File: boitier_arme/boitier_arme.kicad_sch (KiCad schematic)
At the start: 7 parts, among them J1 Conn_01x02_Pin, U1 XIAO-nRF52840-SMD

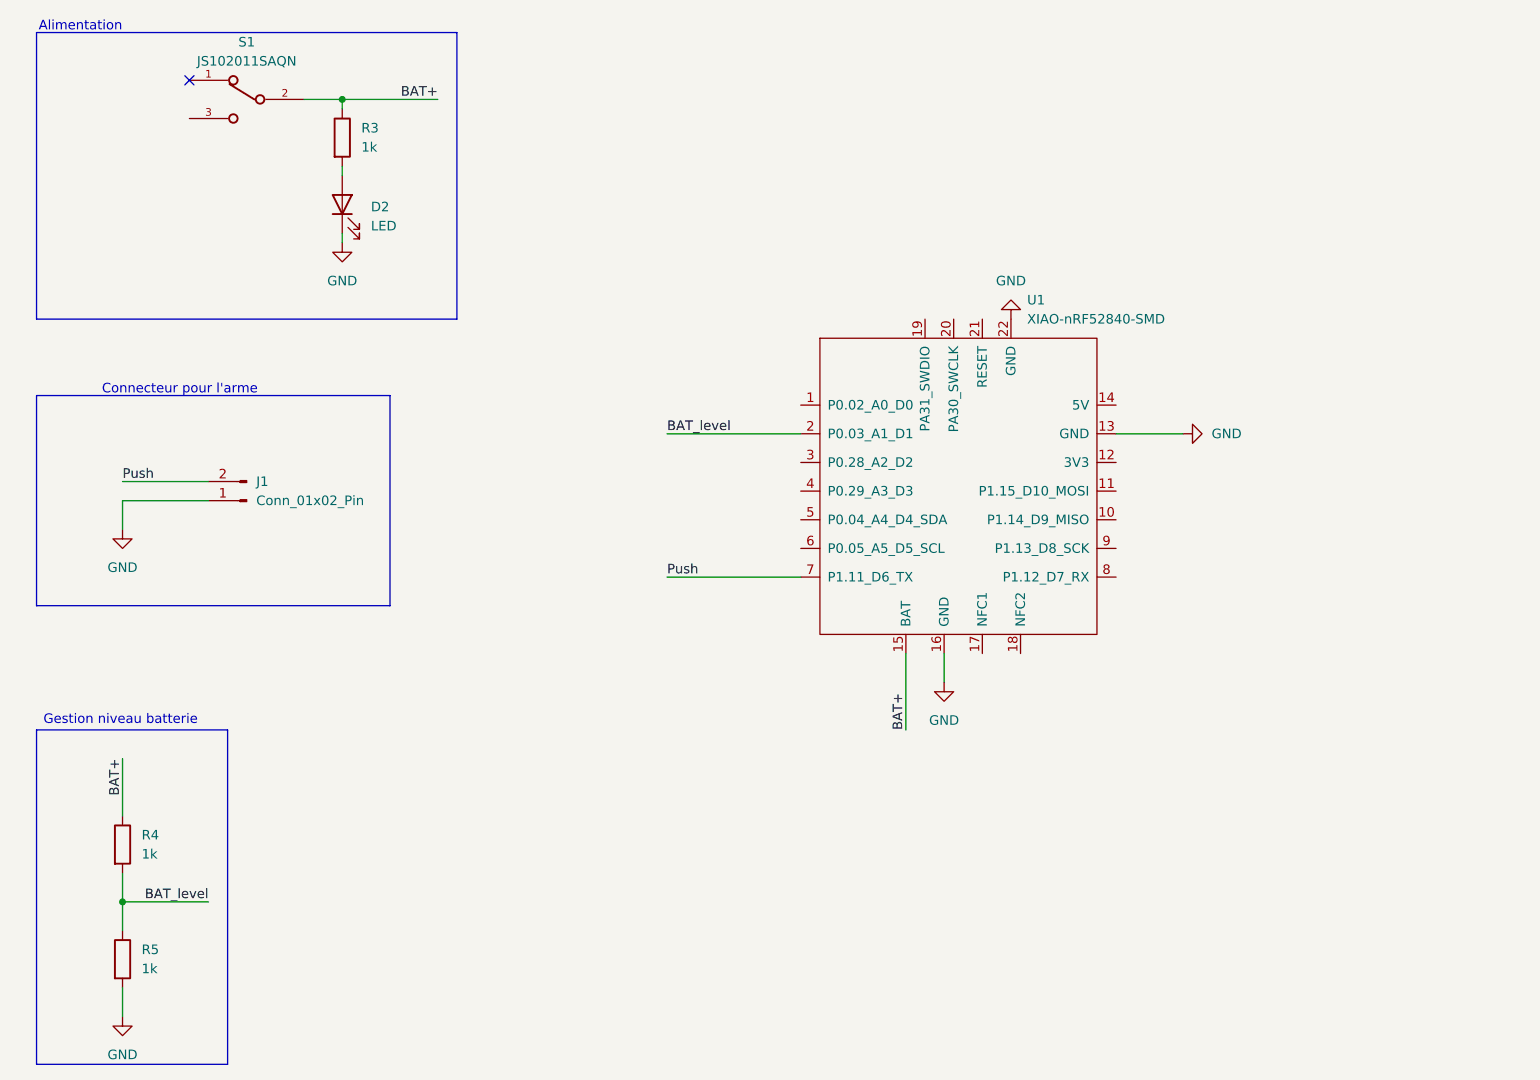
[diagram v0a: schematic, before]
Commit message: batterie rajouté
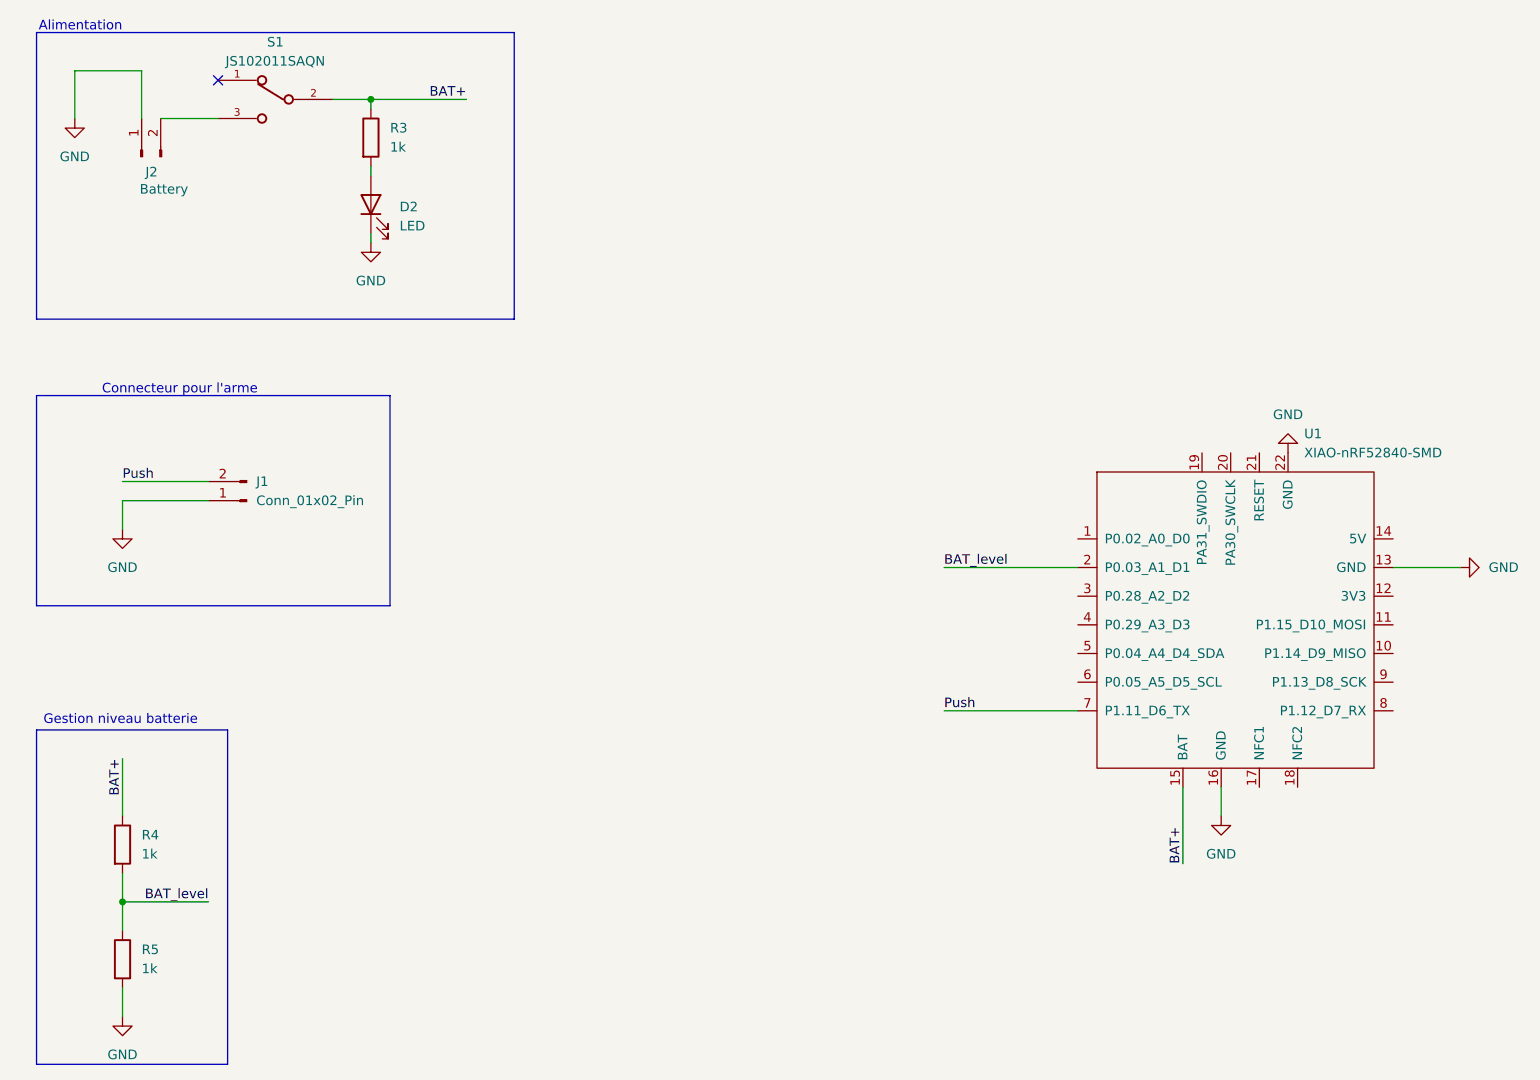
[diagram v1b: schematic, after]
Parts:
- added J2: Battery, Connector_JST:JST_XH_B2B-XH-A_1x02_P2.50mm_Vertical, symbol Connector:Conn_01x02_Pin
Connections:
- net GND: now also J2.1 (Pin_1)
- net at S1.3: now also J2.2 (Pin_2)
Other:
- moved on the sheet: D2, R3, S1, U1

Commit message: a jour
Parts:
- removed J2: Battery, Connector_JST:JST_XH_B2B-XH-A_1x02_P2.50mm_Vertical, symbol Connector:Conn_01x02_Pin
- added J2: 125SH-B-02-TS, CONN_125SH-B-02-TS_ADM, symbol 2025-07-15_01-55-54:125SH-B-02-TS
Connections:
- net GND: now also J2.2
- net at S1.3: now also J2.1
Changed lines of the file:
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@@
+	)
+	(symbol
+		(lib_id "2025-07-15_01-55-54:125SH-B-02-TS")
+		(at 30.48 27.94 270)
+		(unit 1)
+		(exclude_from_sim no)
+		(in_bom yes)
+		(on_board yes)
+		(dnp no)
+		(fields_autoplaced yes)
+		(property "Reference" "J2"
+			(at 34.29 35.5599 90)
+			(effects
+				(font
+					(size 1.524 1.524)
+				)
+				(justify left)
+			)
+		)
+		(property "Value" "125SH-B-02-TS"
+			(at 34.29 38.0999 90)
+			(effects
+				(font
+					(size 1.524 1.524)
+				)
+				(justify left)
+			)
+		)
+		(property "Footprint" "CONN_125SH-B-02-TS_ADM"
+			(at 30.48 27.94 0)
+			(effects
+				(font
+					(size 1.27 1.27)
+					(italic yes)
+				)
+				(hide yes)
+			)
+		)
+		(property "Datasheet" "125SH-B-02-TS"
+			(at 30.48 27.94 0)
+			(effects
+				(font
+					(size 1.27 1.27)
+					(italic yes)
+				)
+				(hide yes)
+			)
+		)
+		(property "Description" ""
+			(at 30.48 27.94 0)
+			(effects
+				(font
+					(size 1.27 1.27)
+				)
+				(hide yes)
+			)
+		)
+		(pin "1"
+		)
+		(pin "2"
+		)
+		(instances
+			(project ""
+				(path "/98d1fd79-24f6-41e8-83f3-a60accf8c857"
+					(reference "J2")
+					(unit 1)
+				)
+			)
+		)
 	)
 	(symbol
@@
 					(unit 1)
 				)
-			)
-		)
-	)
-	(symbol
-		(lib_id "Connector:Conn_01x02_Pin")
-		(at 27.94 33.02 90)
-		(unit 1)
-		(exclude_from_sim no)
-		(in_bom yes)
-		(on_board yes)
-		(dnp no)
-		(property "Reference" "J2"
-			(at 28.448 35.052 90)
-			(effects
-				(font
-					(size 1.27 1.27)
-				)
-				(justify right)
-			)
-		)
-		(property "Value" "Battery"
-			(at 27.686 37.338 90)
-			(effects
-				(font
-					(size 1.27 1.27)
-				)
-				(justify right)
-			)
-		)
-		(property "Footprint" "Connector_JST:JST_XH_B2B-XH-A_1x02_P2.50mm_Vertical"
-			(at 27.94 33.02 0)
-			(effects
-				(font
-					(size 1.27 1.27)
-				)
-				(hide yes)
-			)
-		)
-		(property "Datasheet" "~"
-			(at 27.94 33.02 0)
-			(effects
-				(font
-					(size 1.27 1.27)
-				)
-				(hide yes)
-			)
-		)
-		(property "Description" "Generic connector, single row, 01x02, script generated"
-			(at 27.94 33.02 0)
-			(effects
-				(font
-					(size 1.27 1.27)
-				)
-				(hide yes)
-			)
-		)
-		(pin "1"
-		)
-		(pin "2"
-		)
-		(instances
-			(project "boitier_arme"
-				(path "/98d1fd79-24f6-41e8-83f3-a60accf8c857"
-					(reference "J2")
-					(unit 1)
-				)

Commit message: a jour
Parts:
- J1: footprint Connector_JST:JST_XH_B2B-XH-A_1x02_P2.50mm_Vertical -> Connector_JST:JST_XH_S2B-XH-A-1_1x02_P2.50mm_Horizontal
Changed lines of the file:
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@@
 			)
 		)
-		(property "Footprint" "Connector_JST:JST_XH_B2B-XH-A_1x02_P2.50mm_Vertical"
+		(property "Footprint" "Connector_JST:JST_XH_S2B-XH-A-1_1x02_P2.50mm_Horizontal"
 			(at 41.91 78.74 0)
 			(effects

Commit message: Changement suite au retour du GUS
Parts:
- added H1, H2, H3: MountingHole, MountingHole:MountingHole_3.5mm, symbol Mechanical:MountingHole
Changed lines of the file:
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@@
+	)
+	(symbol
+		(lib_id "Mechanical:MountingHole")
+		(at 92.71 26.67 0)
+		(unit 1)
+		(exclude_from_sim no)
+		(in_bom no)
+		(on_board yes)
+		(dnp no)
+		(fields_autoplaced yes)
+		(property "Reference" "H2"
+			(at 95.25 25.3999 0)
+			(effects
+				(font
+					(size 1.27 1.27)
+				)
+				(justify left)
+			)
+		)
+		(property "Value" "MountingHole"
+			(at 95.25 27.9399 0)
+			(effects
+				(font
+					(size 1.27 1.27)
+				)
+				(justify left)
+			)
+		)
+		(property "Footprint" "MountingHole:MountingHole_3.5mm"
+			(at 92.71 26.67 0)
+			(effects
+				(font
+					(size 1.27 1.27)
+				)
+				(hide yes)
+			)
+		)
+		(property "Datasheet" "~"
+			(at 92.71 26.67 0)
+			(effects
+				(font
+					(size 1.27 1.27)
+				)
+				(hide yes)
+			)
+		)
+		(property "Description" "Mounting Hole without connection"
+			(at 92.71 26.67 0)
+			(effects
+				(font
+					(size 1.27 1.27)
+				)
+				(hide yes)
+			)
+		)
+		(instances
+			(project "boitier_arme"
+				(path "/98d1fd79-24f6-41e8-83f3-a60accf8c857"
+					(reference "H2")
+					(unit 1)
+				)
+			)
+		)
+	)
+	(symbol
+		(lib_id "Mechanical:MountingHole")
+		(at 92.71 21.59 0)
+		(unit 1)
+		(exclude_from_sim no)
+		(in_bom no)
+		(on_board yes)
+		(dnp no)
+		(fields_autoplaced yes)
+		(property "Reference" "H1"
+			(at 95.25 20.3199 0)
+			(effects
+				(font
+					(size 1.27 1.27)
+				)
+				(justify left)
+			)
+		)
+		(property "Value" "MountingHole"
+			(at 95.25 22.8599 0)
+			(effects
+				(font
+					(size 1.27 1.27)
+				)
+				(justify left)
+			)
+		)
+		(property "Footprint" "MountingHole:MountingHole_3.5mm"
+			(at 92.71 21.59 0)
+			(effects
+				(font
+					(size 1.27 1.27)
+				)
+				(hide yes)
+			)
+		)
+		(property "Datasheet" "~"
+			(at 92.71 21.59 0)
+			(effects
+				(font
+					(size 1.27 1.27)
+				)
+				(hide yes)
+			)
+		)
+		(property "Description" "Mounting Hole without connection"
+			(at 92.71 21.59 0)
+			(effects
+				(font
+					(size 1.27 1.27)
+				)
+				(hide yes)
+			)
+		)
+		(instances
+			(project ""
+				(path "/98d1fd79-24f6-41e8-83f3-a60accf8c857"
+					(reference "H1")
+					(unit 1)
+				)
+			)
+		)
 	)
 	(symbol
@@
 					(unit 1)
 				)
+			)
+		)
+	)
+	(symbol
+		(lib_id "Mechanical:MountingHole")
+		(at 92.71 31.75 0)
+		(unit 1)
+		(exclude_from_sim no)
+		(in_bom no)
+		(on_board yes)
+		(dnp no)
+		(fields_autoplaced yes)
+		(property "Reference" "H3"
+			(at 95.25 30.4799 0)
+			(effects
+				(font
+					(size 1.27 1.27)
+				)
+				(justify left)
+			)
+		)
+		(property "Value" "MountingHole"
+			(at 95.25 33.0199 0)
+			(effects
+				(font
+					(size 1.27 1.27)
+				)
+				(justify left)
+			)
+		)
+		(property "Footprint" "MountingHole:MountingHole_3.5mm"
+			(at 92.71 31.75 0)
+			(effects
+				(font
+					(size 1.27 1.27)
+				)
+				(hide yes)
+			)
+		)
+		(property "Datasheet" "~"
+			(at 92.71 31.75 0)
+			(effects
+				(font
+					(size 1.27 1.27)
+				)
+				(hide yes)
+			)
+		)
+		(property "Description" "Mounting Hole without connection"
+			(at 92.71 31.75 0)
+			(effects
+				(font
+					(size 1.27 1.27)
+				)
+				(hide yes)
+			)
+		)
+		(instances
+			(project "boitier_arme"
+				(path "/98d1fd79-24f6-41e8-83f3-a60accf8c857"
+					(reference "H3")
+					(unit 1)
+				)
